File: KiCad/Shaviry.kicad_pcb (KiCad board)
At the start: 2 copper layers, 40.5 x 67.6 mm, 29 parts, among them J1 AMIGA_DB23_RGB_ENTRADA_HEMBRA, J2 VGA_SALIDA_HEMBRA, J3 VGA_ENTRADA_HEMBRA, J4 Conn_02x03_Top_Bottom, J5 Conn_01x03_Pin, U1 74HCT14, U3 THS7374, U5 PC817

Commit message: Add files via upload
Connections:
- J2 pad 0: GND -> (no net)
- J3 pad 0: GND -> (no net)
- R4 pad 1: Net-(U3-CH1_OUT) -> Net-(U3-CH2_OUT)
- R5 pad 1: Net-(U3-CH2_OUT) -> Net-(U3-CH3_OUT)
- R6 pad 1: Net-(U3-CH3_OUT) -> Net-(U3-CH4_OUT)
- U3 pad 1: Net-(J1-RED) -> unconnected-(U3-CH1_IN-Pad1)
- U3 pad 11: unconnected-(U3-CH4_OUT-Pad11) -> Net-(U3-CH4_OUT)
- U3 pad 14: Net-(U3-CH1_OUT) -> unconnected-(U3-CH1_OUT-Pad14)
- U3 pad 2: Net-(J1-GREEN) -> Net-(J1-RED)
- U3 pad 3: Net-(J1-BLUE) -> Net-(J1-GREEN)
- U3 pad 4: unconnected-(U3-CH4_IN-Pad4) -> Net-(J1-BLUE)
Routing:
- net Net-(U3-CH4_OUT): track 0.00 -> 4.56 mm
- net Net-(U3-CH1_OUT): track 4.20 -> 0.00 mm
- net Net-(U3-CH3_OUT): track 5.59 -> 3.62 mm
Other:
- board text added: "SHAVIRY REV:02012024"
- board text removed: "SHAVIRY REV:19122023"

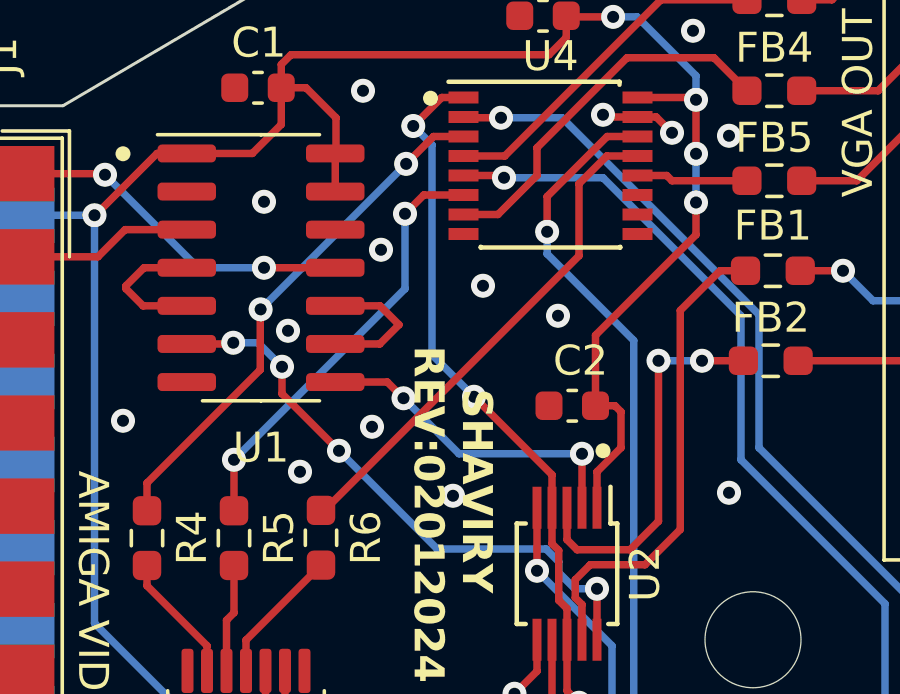
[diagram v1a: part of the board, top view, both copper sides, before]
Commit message: Add files via upload
Cambiada la fecha en la serigrafía inferior
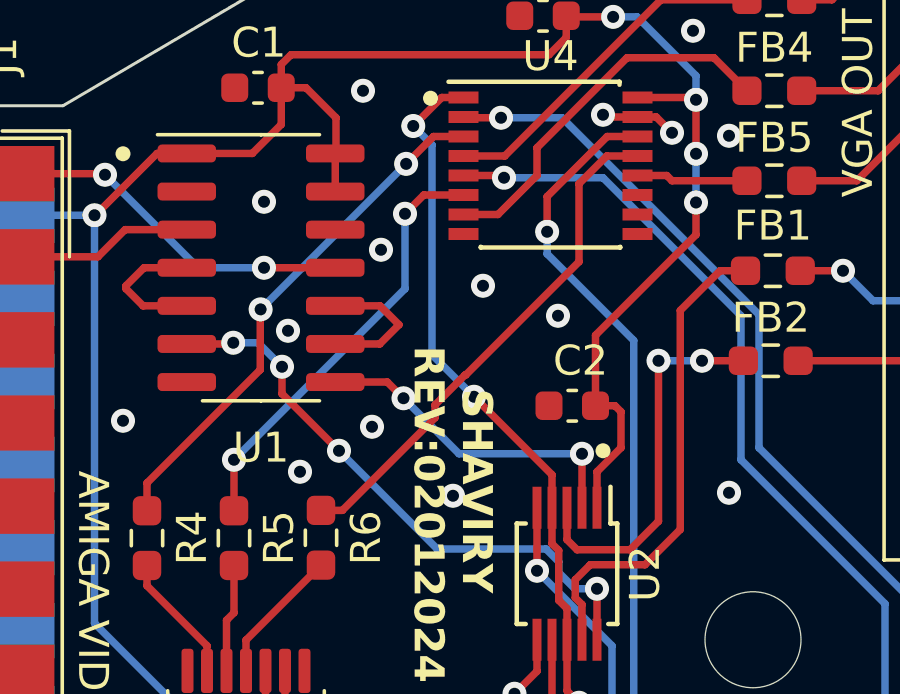
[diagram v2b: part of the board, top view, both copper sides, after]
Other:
- board text added: "2023-24 Anubis (Enrique Ferrari Lorenzo)"
- board text removed: "2023 Anubis (Enrique Ferrari Lorenzo)"
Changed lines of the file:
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@@
     (effects (font (size 1 1) (thickness 0.15)) (justify left bottom mirror))
   )
-  (gr_text "2023 Anubis (Enrique Ferrari Lorenzo)" (at 156.7 103.145 270) (layer "B.SilkS")
+  (gr_text "2023-24 Anubis (Enrique Ferrari Lorenzo)" (at 156.7 104.445 270) (layer "B.SilkS")
     (effects (font (size 1 1) (thickness 0.15)) (justify left bottom mirror))
   )
@@
   (segment (start 151.86 107.565) (end 147.2075 107.565) (width 0.25) (layer "F.Cu") (net 53))
   (segment (start 147.2075 107.565) (end 147.2 107.5575) (width 0.25) (layer "F.Cu") (net 53))
-  (segment (start 148.1 75.145) (end 148.1 72.745) (width 0.25) (layer "F.Cu") (net 54))
+  (segment (start 144.325 79.12) (end 148.1 75.345) (width 0.25) (layer "F.Cu") (net 54))
+  (segment (start 140.2125 83.6325) (end 143.3 80.545) (width 0.25) (layer "F.Cu") (net 54))
+  (segment (start 149.025 71.82) (end 150.05 71.82) (width 0.25) (layer "F.Cu") (net 54))
+  (segment (start 143.3 80.545) (end 143.3 80.119695) (width 0.25) (layer "F.Cu") (net 54))
+  (segment (start 144.299695 79.12) (end 144.325 79.12) (width 0.25) (layer "F.Cu") (net 54))
+  (segment (start 143.3 80.119695) (end 144.299695 79.12) (width 0.25) (layer "F.Cu") (net 54))
   (segment (start 148.1 72.745) (end 149.025 71.82) (width 0.25) (layer "F.Cu") (net 54))
-  (segment (start 139.6125 83.6325) (end 148.1 75.145) (width 0.25) (layer "F.Cu") (net 54))
-  (segment (start 149.025 71.82) (end 150.05 71.82) (width 0.25) (layer "F.Cu") (net 54))
-  (segment (start 139.5 83.6325) (end 139.6125 83.6325) (width 0.25) (layer "F.Cu") (net 54))
+  (segment (start 139.5 83.6325) (end 140.2125 83.6325) (width 0.25) (layer "F.Cu") (net 54))
+  (segment (start 148.1 75.345) (end 148.1 72.745) (width 0.25) (layer "F.Cu") (net 54))
   (segment (start 133 76.245) (end 133.57 76.815) (width 0.25) (layer "F.Cu") (net 56))
   (segment (start 133.57 76.815) (end 135.025 76.815) (width 0.25) (layer "F.Cu") (net 56))

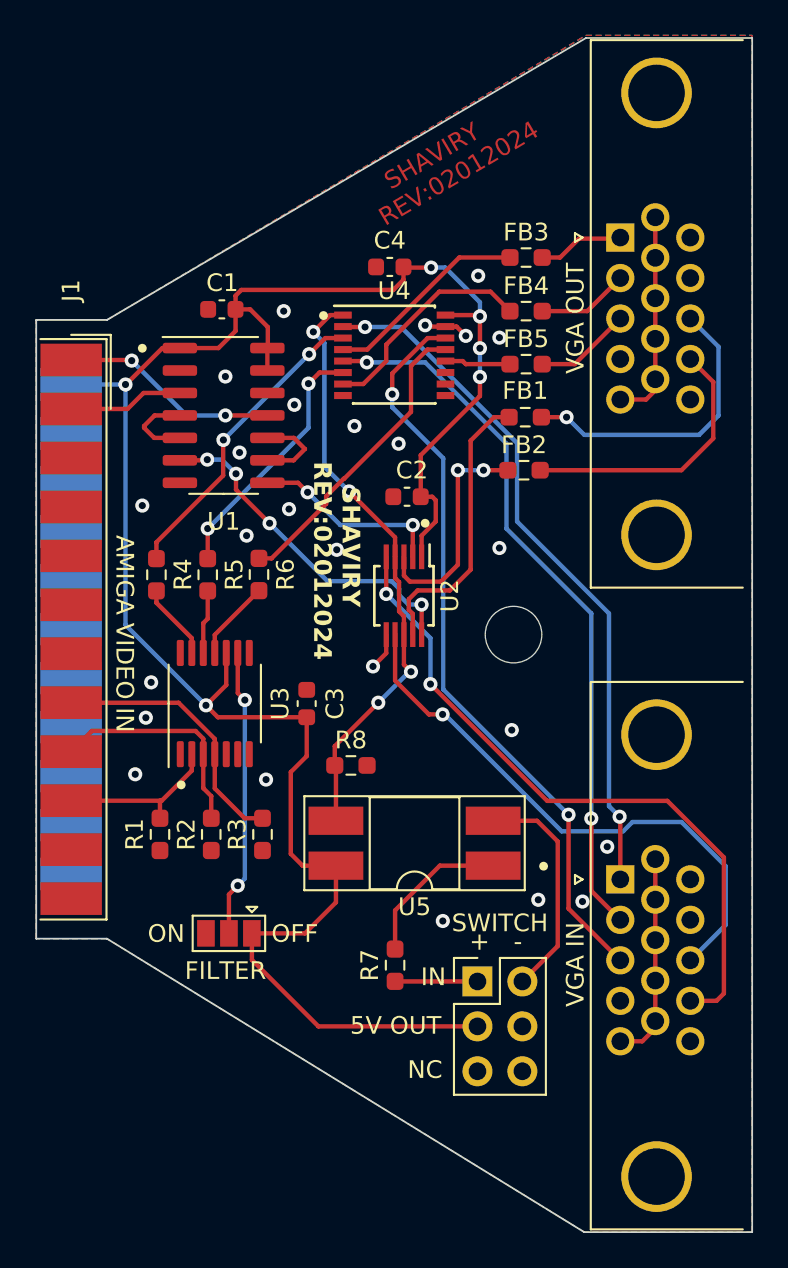
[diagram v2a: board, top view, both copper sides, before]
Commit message: Add files via upload
Cambiado el punto de conexión de la pista de la entrada G del RGB del Amiga al amplificador. No hay cambios en funcionalidad ya que va al mismo sítio pero por otro lado.
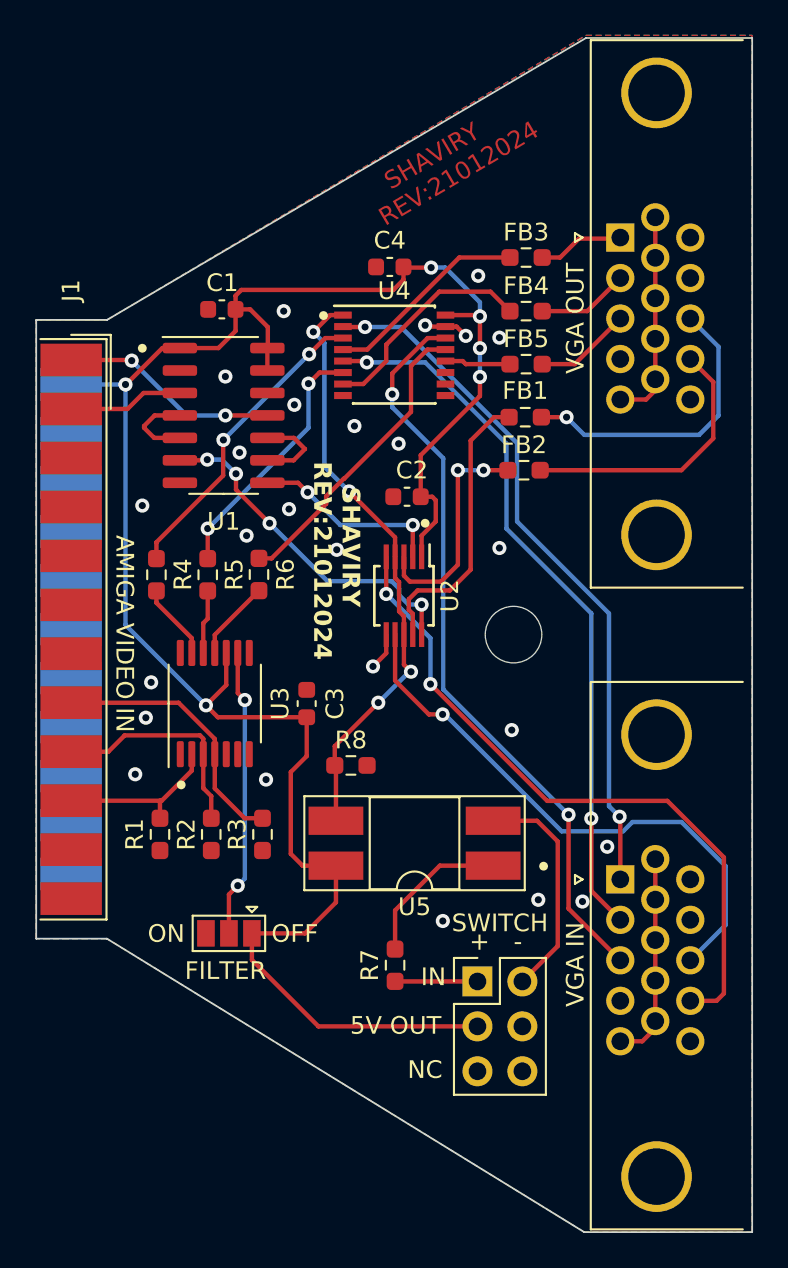
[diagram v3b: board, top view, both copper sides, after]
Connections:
- J2 pad 0: (no net) -> GND
- J3 pad 0: (no net) -> GND
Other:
- board text added: "SHAVIRY REV:21012024"
- board text removed: "SHAVIRY REV:02012024"
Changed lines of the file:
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@@
     (fp_arc (start 6.585 2.05) (mid 8.185 0.45) (end 9.785 2.05)
       (stroke (width 0.1) (type solid)) (layer "F.Fab"))
-    (pad "0" thru_hole circle (at -16.815 2.05 90) (size 4 4) (drill 3.2) (layers "*.Cu" "*.Mask"))
-    (pad "0" thru_hole circle (at 8.185 2.05 90) (size 4 4) (drill 3.2) (layers "*.Cu" "*.Mask"))
+    (pad "0" thru_hole circle (at -16.815 2.05 90) (size 4 4) (drill 3.2) (layers "*.Cu" "*.Mask")
+      (net 5 "GND"))
+    (pad "0" thru_hole circle (at 8.185 2.05 90) (size 4 4) (drill 3.2) (layers "*.Cu" "*.Mask")
+      (net 5 "GND"))
     (pad "1" thru_hole rect (at 0 0 90) (size 1.6 1.6) (drill 1) (layers "*.Cu" "*.Mask")
       (net 1 "Net-(FB3-Pad2)") (pintype "passive"))
@@
     (fp_arc (start 6.585 2.05) (mid 8.185 0.45) (end 9.785 2.05)
       (stroke (width 0.1) (type solid)) (layer "F.Fab"))
-    (pad "0" thru_hole circle (at -16.815 2.05 90) (size 4 4) (drill 3.2) (layers "*.Cu" "*.Mask"))
-    (pad "0" thru_hole circle (at 8.185 2.05 90) (size 4 4) (drill 3.2) (layers "*.Cu" "*.Mask"))
+    (pad "0" thru_hole circle (at -16.815 2.05 90) (size 4 4) (drill 3.2) (layers "*.Cu" "*.Mask")
+      (net 5 "GND"))
+    (pad "0" thru_hole circle (at 8.185 2.05 90) (size 4 4) (drill 3.2) (layers "*.Cu" "*.Mask")
+      (net 5 "GND"))
     (pad "1" thru_hole rect (at 0 0 90) (size 1.6 1.6) (drill 1) (layers "*.Cu" "*.Mask")
       (net 23 "Net-(U4-S1A)") (pintype "passive"))
@@
     )
     (stroke (width 0.1) (type solid)) (fill none) (layer "Edge.Cuts"))
-  (gr_text "   SHAVIRY\nREV:02012024" (at 146.7 64.945 30.5) (layer "F.Cu" knockout)
+  (gr_text "   SHAVIRY\nREV:21012024" (at 146.7 64.945 30.5) (layer "F.Cu" knockout)
     (effects (font (size 1 1) (thickness 0.15)) (justify left bottom))
   )
@@
     (effects (font (size 1 1) (thickness 0.15)) (justify left bottom))
   )
-  (gr_text "   SHAVIRY\nREV:02012024" (at 142.5 78.145 270) (layer "F.SilkS")
+  (gr_text "   SHAVIRY\nREV:21012024" (at 142.5 78.145 270) (layer "F.SilkS")
     (effects (font (size 1 1) (thickness 0.25) bold) (justify left bottom))
   )
@@
   (segment (start 133.9 98.3325) (end 133.9 97.34) (width 0.25) (layer "F.Cu") (net 19))
   (segment (start 136.35 96.631396) (end 136.35 94.7075) (width 0.25) (layer "F.Cu") (net 20))
-  (segment (start 136.8 97.081396) (end 136.35 96.631396) (width 0.25) (layer "F.Cu") (net 20))
   (segment (start 136.35 94.7075) (end 136.35 93.831396) (width 0.25) (layer "F.Cu") (net 20))
-  (segment (start 136.35 93.831396) (end 135.913604 93.395) (width 0.25) (layer "F.Cu") (net 20))
-  (segment (start 130.05 93.395) (end 128.875 94.57) (width 0.25) (layer "F.Cu") (net 20))
+  (segment (start 136.8 97.081396) (end 136.35 96.631396) (width 0.25) (layer "F.Cu") (net 20))
+  (segment (start 136.35 93.831396) (end 136.163604 93.645) (width 0.25) (layer "F.Cu") (net 20))
+  (segment (start 130.975 94.57) (end 128.875 94.57) (width 0.25) (layer "F.Cu") (net 20))
+  (segment (start 131.9 93.645) (end 130.975 94.57) (width 0.25) (layer "F.Cu") (net 20))
   (segment (start 136.8 98.3325) (end 136.8 97.081396) (width 0.25) (layer "F.Cu") (net 20))
-  (segment (start 135.913604 93.395) (end 130.05 93.395) (width 0.25) (layer "F.Cu") (net 20))
+  (segment (start 136.163604 93.645) (end 131.9 93.645) (width 0.25) (layer "F.Cu") (net 20))
   (segment (start 152.598406 68.545) (end 153.698406 69.645) (width 0.25) (layer "F.Cu") (net 21))
   (segment (start 145.399805 73.77) (end 146.7 72.469805) (width 0.25) (layer "F.Cu") (net 21))
